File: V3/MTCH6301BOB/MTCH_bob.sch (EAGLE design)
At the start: 22 parts, among them J2 LiPo, U2 MTCH6301-I/ML, U4 AP2112K-3.3TRG-1

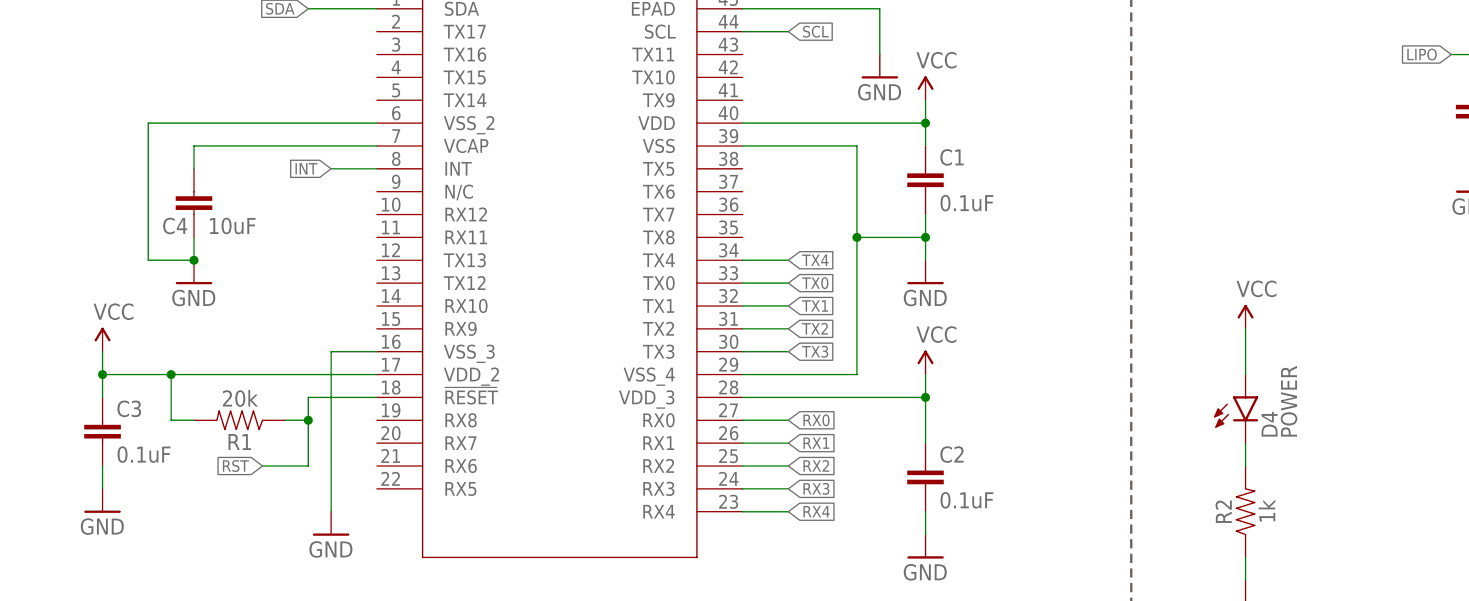
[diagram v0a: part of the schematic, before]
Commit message: updated MTCH6301 breakout board because of out of stock parts
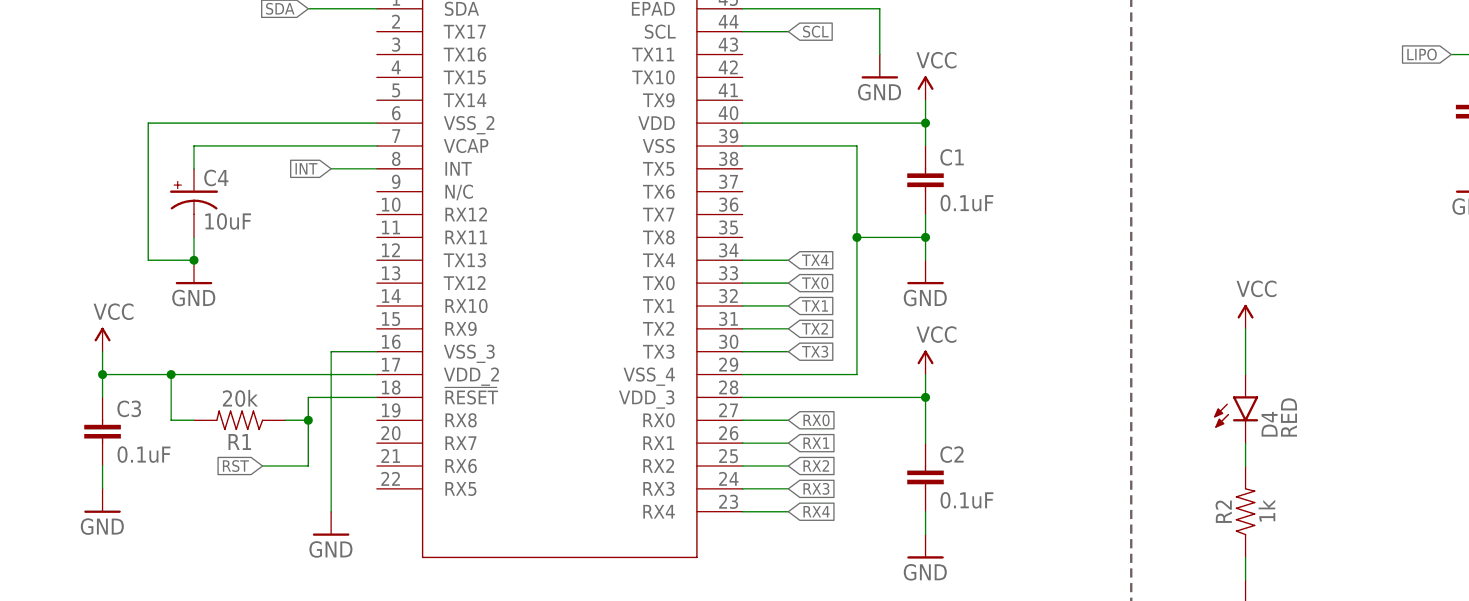
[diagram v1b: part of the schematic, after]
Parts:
- C4: device SparkFun-Capacitors:10UF-0603-6.3V-20% -> SparkFun-Capacitors:10UF-POLAR-EIA3528-20V-10%(TANT)
- D4: value POWER -> RED; device SparkFun-LED:LED-GREEN0603 -> SparkFun-LED:LED-RED1206; PROD_ID DIO-00821 -> (none)
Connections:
- net GND: now also C4.-; no longer C4.2
- net N$2: now also C4.+; no longer C4.1
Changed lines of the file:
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@@
 <part name="C2" library="SparkFun-Capacitors" library_urn="urn:adsk.eagle:library:510" deviceset="0.1UF" device="-0603-25V-(+80/-20%)" package3d_urn="urn:adsk.eagle:package:37414/1" value="0.1uF"/>
 <part name="C3" library="SparkFun-Capacitors" library_urn="urn:adsk.eagle:library:510" deviceset="0.1UF" device="-0603-25V-(+80/-20%)" package3d_urn="urn:adsk.eagle:package:37414/1" value="0.1uF"/>
-<part name="C4" library="SparkFun-Capacitors" library_urn="urn:adsk.eagle:library:510" deviceset="10UF" device="-0603-6.3V-20%" package3d_urn="urn:adsk.eagle:package:37414/1" value="10uF"/>
 <part name="GND2" library="SparkFun" deviceset="GND" device=""/>
 <part name="P+1" library="SFE Aesthetics" deviceset="VCC" device=""/>
@@
 <part name="SUPPLY2" library="SparkFun-PowerSymbols" library_urn="urn:adsk.eagle:library:530" deviceset="VOUT" device=""/>
 <part name="P+5" library="SFE Aesthetics" deviceset="VCC" device=""/>
-<part name="D4" library="SparkFun-LED" deviceset="LED-GREEN" device="0603" value="POWER">
-<attribute name="PROD_ID" value="DIO-00821"/>
-</part>
+<part name="D4" library="SparkFun-LED" library_urn="urn:adsk.eagle:library:529" deviceset="LED-RED" device="1206" package3d_urn="urn:adsk.eagle:package:39352/1" value="RED"/>
 <part name="P+6" library="SFE Aesthetics" deviceset="VCC" device=""/>
 <part name="GND10" library="SFE Aesthetics" deviceset="GND" device=""/>
 <part name="R2" library="SparkFun-Resistors" deviceset="1KOHM" device="-0603-1/10W-1%" value="1k"/>
+<part name="C4" library="SparkFun-Capacitors" library_urn="urn:adsk.eagle:library:510" deviceset="10UF-POLAR" device="-EIA3528-20V-10%(TANT)" package3d_urn="urn:adsk.eagle:package:37411/1" value="10uF"/>
 </parts>
 <sheets>
@@
 <attribute name="VALUE" x="29.464" y="109.601" size="1.778" layer="96" font="vector"/>
 </instance>
-<instance part="C4" gate="G$1" x="38.1" y="137.16" smashed="yes">
-<attribute name="NAME" x="34.544" y="135.001" size="1.778" layer="95" font="vector"/>
-<attribute name="VALUE" x="39.624" y="135.001" size="1.778" layer="96" font="vector"/>
-</instance>
 <instance part="GND2" gate="1" x="38.1" y="129.54" smashed="yes">
 <attribute name="VALUE" x="35.56" y="127" size="1.778" layer="96"/>
@@
 <attribute name="NAME" x="153.416" y="104.14" size="1.778" layer="95" font="vector" rot="R90" align="bottom-center"/>
 <attribute name="VALUE" x="156.464" y="104.14" size="1.778" layer="96" font="vector" rot="R90" align="top-center"/>
+</instance>
+<instance part="C4" gate="G$1" x="38.1" y="139.7" smashed="yes">
+<attribute name="NAME" x="39.116" y="140.335" size="1.778" layer="95" font="vector"/>
+<attribute name="VALUE" x="39.116" y="135.509" size="1.778" layer="96" font="vector"/>
 </instance>
 </instances>
@@
 </segment>
 <segment>
-<pinref part="C4" gate="G$1" pin="2"/>
 <wire x1="38.1" y1="134.62" x2="38.1" y2="132.08" width="0.1524" layer="91"/>
 <pinref part="GND2" gate="1" pin="GND"/>
@@
 <wire x1="33.02" y1="132.08" x2="38.1" y2="132.08" width="0.1524" layer="91"/>
 <junction x="38.1" y="132.08"/>
+<pinref part="C4" gate="G$1" pin="-"/>
 </segment>
 <segment>
@@
 <pinref part="U2" gate="A" pin="VCAP"/>
 <wire x1="58.42" y1="144.78" x2="38.1" y2="144.78" width="0.1524" layer="91"/>
-<pinref part="C4" gate="G$1" pin="1"/>
 <wire x1="38.1" y1="144.78" x2="38.1" y2="142.24" width="0.1524" layer="91"/>
-</segment>
-</net>
+<pinref part="C4" gate="G$1" pin="+"/>
+</segment>
+</net>
